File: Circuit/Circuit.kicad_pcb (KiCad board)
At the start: 2 copper layers, 113 x 36.8 mm, 30 parts, among them J1 UE27AC54100, J2 22-23-2021, J3 22-23-2021, J4 22-23-2021, J5 22-23-2021, J6 22-23-2021, J7 22-23-2021, Q1 AO3401A, Q2 2N2222A, U1 L4978

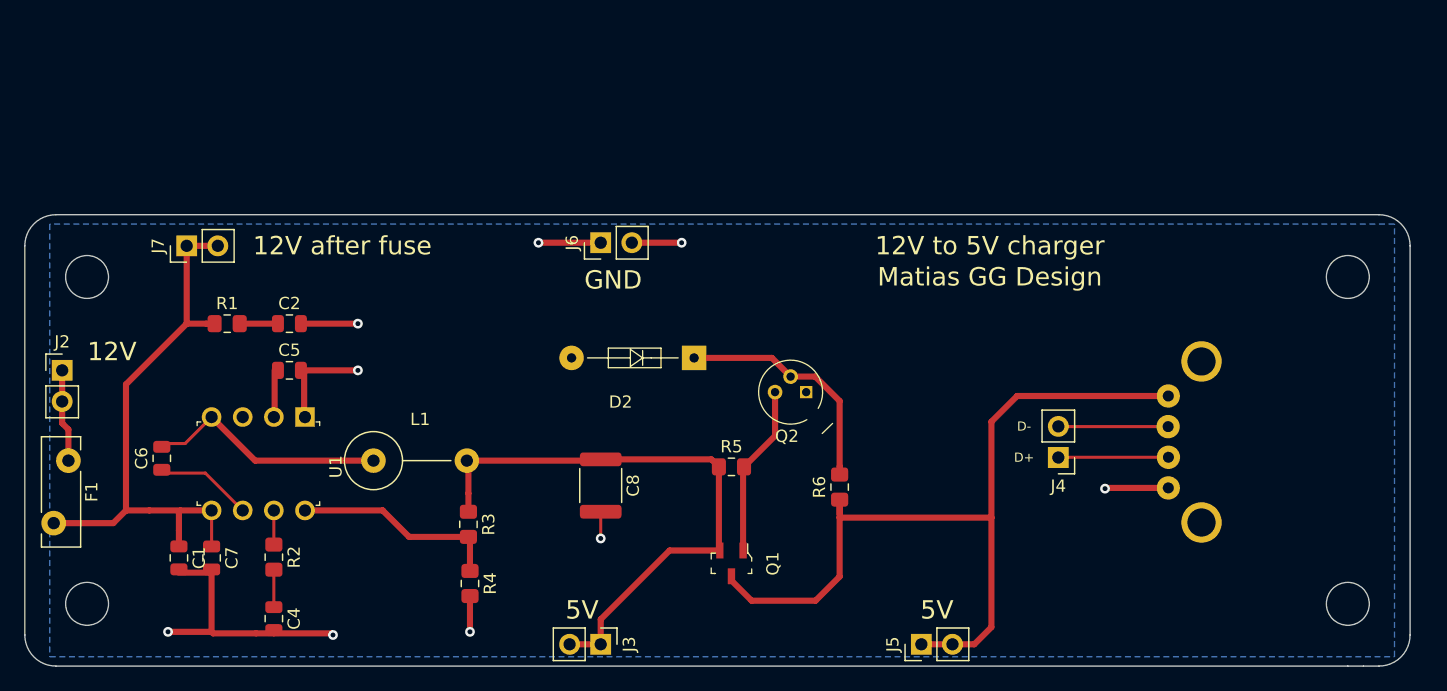
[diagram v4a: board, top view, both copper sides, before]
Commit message: Updated board, shorter board
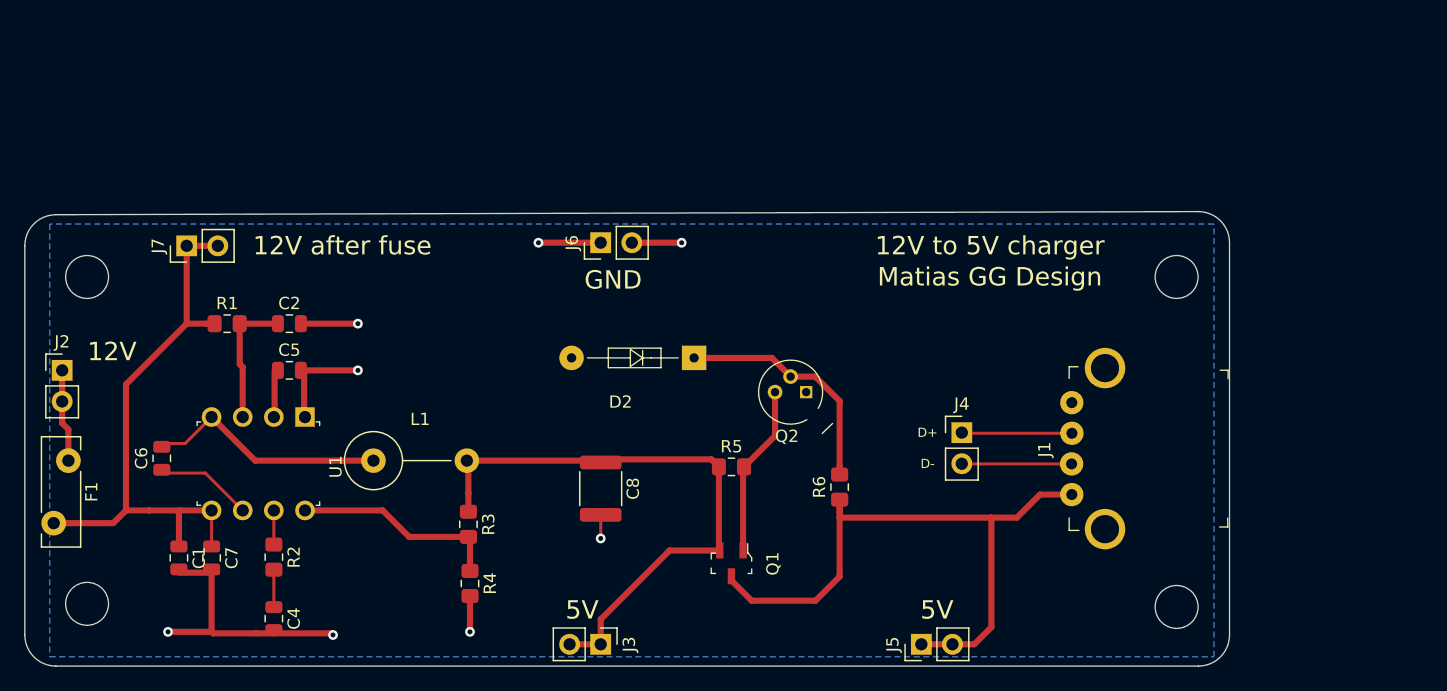
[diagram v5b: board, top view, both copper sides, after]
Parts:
- J1: moved to F.Cu
- moved Mnt4 14.0 mm to (167.9, 116.1)
- moved Mnt3 14.0 mm to (167.9, 89.2)
- moved J4 8.13 mm to (150.4, 101.9), turned to 0 degrees
- moved J1 7.89 mm to (162.1, 103.2), turned to 90 degrees
- moved C8 0.25 mm to (120.9, 106.4)
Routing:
- net Net-(J1-Pad1): track 68.9 -> 53.1 mm
- net Net-(C2-Pad1): track 3.20 -> 10.9 mm
- net GND: track 53.2 -> 48.0 mm, vias 9 -> 8
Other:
- board size 113 x 36.8 mm -> 98.3 x 37.1 mm
